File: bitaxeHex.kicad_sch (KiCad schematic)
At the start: 26 parts, among them J1 Screw Terminal, J2 Screw Terminal

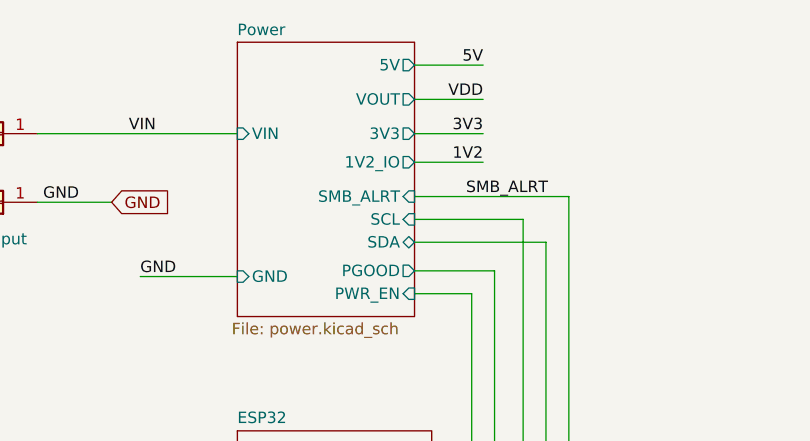
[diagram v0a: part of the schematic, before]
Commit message: -Reset to 1V8/0V8 setup -Add TVS protection
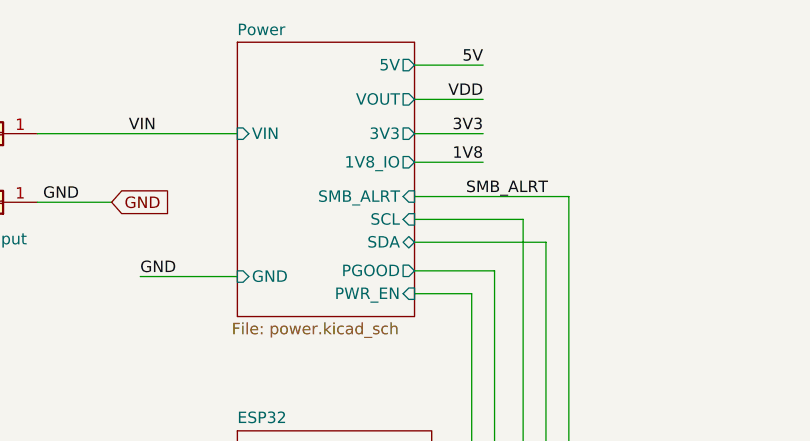
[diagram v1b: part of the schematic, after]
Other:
- sheet Power ports: added 1V8_IO; removed 1V2_IO
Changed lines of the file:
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@@
 		)
 	)
-	(label "1V2"
+	(label "1V8"
 		(at 86.995 36.195 180)
 		(fields_autoplaced yes)
@@
 			)
 		)
-		(pin "1V2_IO" output
+		(pin "1V8_IO" output
 			(at 79.375 36.195 0)
 			(effects
